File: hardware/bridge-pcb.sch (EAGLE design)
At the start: 22 parts, among them IC1 MC34063AP, IC2 MAX3232CPE, J1 RJ11, J2 RJ9PTH, M1 ESP01

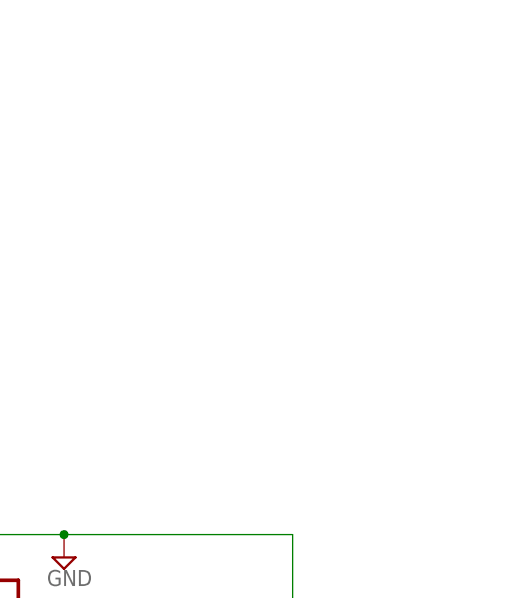
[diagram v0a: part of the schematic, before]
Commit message: Added pin header footprint to provide support for the ESP8266 module
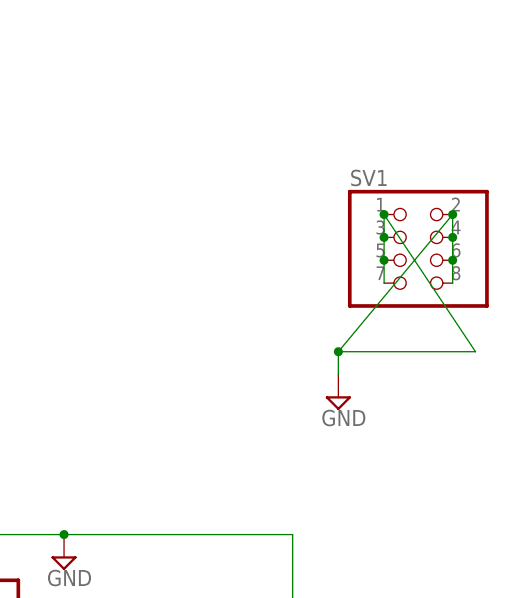
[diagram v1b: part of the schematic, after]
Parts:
- added SV1: (no value), pinhead:PINHD-2X4
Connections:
- net GND: now also SV1.1, SV1.2, SV1.3, SV1.4, SV1.5, SV1.6, SV1.7, SV1.8
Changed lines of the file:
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@@
 <grid distance="0.1" unitdist="inch" unit="inch" style="lines" multiple="1" display="no" altdistance="0.01" altunitdist="inch" altunit="inch"/>
 <layers>
-<layer number="1" name="Top" color="4" fill="1" visible="yes" active="no"/>
-<layer number="16" name="Bottom" color="1" fill="1" visible="yes" active="no"/>
-<layer number="17" name="Pads" color="2" fill="1" visible="yes" active="no"/>
-<layer number="18" name="Vias" color="2" fill="1" visible="yes" active="no"/>
-<layer number="19" name="Unrouted" color="6" fill="1" visible="yes" active="no"/>
-<layer number="20" name="Dimension" color="15" fill="1" visible="yes" active="no"/>
-<layer number="21" name="tPlace" color="7" fill="1" visible="yes" active="no"/>
-<layer number="22" name="bPlace" color="7" fill="1" visible="yes" active="no"/>
-<layer number="23" name="tOrigins" color="15" fill="1" visible="yes" active="no"/>
-<layer number="24" name="bOrigins" color="15" fill="1" visible="yes" active="no"/>
-<layer number="25" name="tNames" color="7" fill="1" visible="yes" active="no"/>
-<layer number="26" name="bNames" color="7" fill="1" visible="yes" active="no"/>
-<layer number="27" name="tValues" color="7" fill="1" visible="yes" active="no"/>
-<layer number="28" name="bValues" color="7" fill="1" visible="yes" active="no"/>
+<layer number="1" name="Top" color="4" fill="1" visible="no" active="no"/>
+<layer number="16" name="Bottom" color="1" fill="1" visible="no" active="no"/>
+<layer number="17" name="Pads" color="2" fill="1" visible="no" active="no"/>
+<layer number="18" name="Vias" color="2" fill="1" visible="no" active="no"/>
+<layer number="19" name="Unrouted" color="6" fill="1" visible="no" active="no"/>
+<layer number="20" name="Dimension" color="15" fill="1" visible="no" active="no"/>
+<layer number="21" name="tPlace" color="7" fill="1" visible="no" active="no"/>
+<layer number="22" name="bPlace" color="7" fill="1" visible="no" active="no"/>
+<layer number="23" name="tOrigins" color="15" fill="1" visible="no" active="no"/>
+<layer number="24" name="bOrigins" color="15" fill="1" visible="no" active="no"/>
+<layer number="25" name="tNames" color="7" fill="1" visible="no" active="no"/>
+<layer number="26" name="bNames" color="7" fill="1" visible="no" active="no"/>
+<layer number="27" name="tValues" color="7" fill="1" visible="no" active="no"/>
+<layer number="28" name="bValues" color="7" fill="1" visible="no" active="no"/>
 <layer number="29" name="tStop" color="7" fill="3" visible="no" active="no"/>
 <layer number="30" name="bStop" color="7" fill="6" visible="no" active="no"/>
@@
 <layer number="35" name="tGlue" color="7" fill="4" visible="no" active="no"/>
 <layer number="36" name="bGlue" color="7" fill="5" visible="no" active="no"/>
-<layer number="37" name="tTest" color="7" fill="1" visible="yes" active="no"/>
-<layer number="38" name="bTest" color="7" fill="1" visible="yes" active="no"/>
+<layer number="37" name="tTest" color="7" fill="1" visible="no" active="no"/>
+<layer number="38" name="bTest" color="7" fill="1" visible="no" active="no"/>
 <layer number="39" name="tKeepout" color="4" fill="11" visible="no" active="no"/>
 <layer number="40" name="bKeepout" color="1" fill="11" visible="no" active="no"/>
@@
 <layer number="44" name="Drills" color="7" fill="1" visible="no" active="no"/>
 <layer number="45" name="Holes" color="7" fill="1" visible="no" active="no"/>
-<layer number="46" name="Milling" color="3" fill="1" visible="yes" active="no"/>
-<layer number="47" name="Measures" color="7" fill="1" visible="yes" active="no"/>
-<layer number="48" name="Document" color="7" fill="1" visible="yes" active="no"/>
-<layer number="49" name="Reference" color="7" fill="1" visible="yes" active="no"/>
-<layer number="50" name="dxf" color="7" fill="1" visible="yes" active="no"/>
-<layer number="51" name="tDocu" color="7" fill="1" visible="yes" active="no"/>
-<layer number="52" name="bDocu" color="7" fill="1" visible="yes" active="no"/>
-<layer number="53" name="tGND_GNDA" color="7" fill="9" visible="yes" active="no"/>
-<layer number="54" name="bGND_GNDA" color="1" fill="9" visible="yes" active="no"/>
-<layer number="56" name="wert" color="7" fill="1" visible="yes" active="no"/>
-<layer number="57" name="tCAD" color="7" fill="1" visible="yes" active="no"/>
+<layer number="46" name="Milling" color="3" fill="1" visible="no" active="no"/>
+<layer number="47" name="Measures" color="7" fill="1" visible="no" active="no"/>
+<layer number="48" name="Document" color="7" fill="1" visible="no" active="no"/>
+<layer number="49" name="Reference" color="7" fill="1" visible="no" active="no"/>
+<layer number="50" name="dxf" color="7" fill="1" visible="no" active="no"/>
+<layer number="51" name="tDocu" color="7" fill="1" visible="no" active="no"/>
+<layer number="52" name="bDocu" color="7" fill="1" visible="no" active="no"/>
+<layer number="53" name="tGND_GNDA" color="7" fill="9" visible="no" active="no"/>
+<layer number="54" name="bGND_GNDA" color="1" fill="9" visible="no" active="no"/>
+<layer number="56" name="wert" color="7" fill="1" visible="no" active="no"/>
+<layer number="57" name="tCAD" color="7" fill="1" visible="no" active="no"/>
 <layer number="90" name="Modules" color="5" fill="1" visible="yes" active="yes"/>
 <layer number="91" name="Nets" color="2" fill="1" visible="yes" active="yes"/>
@@
 </part>
 <part name="LOGO1" library="SparkFun-Aesthetics" deviceset="OSHW-LOGO" device="M"/>
+<part name="SV1" library="pinhead" deviceset="PINHD-2X4" device=""/>
+<part name="SUPPLY13" library="supply2" deviceset="GND" device=""/>
 </parts>
 <sheets>
@@
 </instance>
 <instance part="LOGO1" gate="G$1" x="66.04" y="76.2"/>
+<instance part="SV1" gate="A" x="127" y="66.04"/>
+<instance part="SUPPLY13" gate="GND" x="119.38" y="50.8"/>
 </instances>
 <busses>
@@
 <junction x="88.9" y="35.56"/>
 </segment>
+<segment>
+<pinref part="SUPPLY13" gate="GND" pin="GND"/>
+<pinref part="SV1" gate="A" pin="8"/>
+<wire x1="119.38" y1="53.34" x2="119.38" y2="55.88" width="0.1524" layer="91"/>
+<pinref part="SV1" gate="A" pin="7"/>
+<wire x1="119.38" y1="55.88" x2="132.08" y2="71.12" width="0.1524" layer="91"/>
+<wire x1="132.08" y1="71.12" x2="132.08" y2="68.58" width="0.1524" layer="91"/>
+<wire x1="132.08" y1="68.58" x2="132.08" y2="66.04" width="0.1524" layer="91"/>
+<wire x1="132.08" y1="66.04" x2="132.08" y2="63.5" width="0.1524" layer="91"/>
+<wire x1="124.46" y1="63.5" x2="124.46" y2="66.04" width="0.1524" layer="91"/>
+<wire x1="124.46" y1="66.04" x2="124.46" y2="68.58" width="0.1524" layer="91"/>
+<wire x1="124.46" y1="68.58" x2="124.46" y2="71.12" width="0.1524" layer="91"/>
+<wire x1="124.46" y1="71.12" x2="134.62" y2="55.88" width="0.1524" layer="91"/>
+<wire x1="134.62" y1="55.88" x2="119.38" y2="55.88" width="0.1524" layer="91"/>
+<junction x="119.38" y="55.88"/>
+<pinref part="SV1" gate="A" pin="2"/>
+<junction x="132.08" y="71.12"/>
+<pinref part="SV1" gate="A" pin="4"/>
+<junction x="132.08" y="68.58"/>
+<pinref part="SV1" gate="A" pin="6"/>
+<junction x="132.08" y="66.04"/>
+<pinref part="SV1" gate="A" pin="5"/>
+<junction x="124.46" y="66.04"/>
+<pinref part="SV1" gate="A" pin="3"/>
+<junction x="124.46" y="68.58"/>
+<pinref part="SV1" gate="A" pin="1"/>
+<junction x="124.46" y="71.12"/>
+</segment>
 </net>
